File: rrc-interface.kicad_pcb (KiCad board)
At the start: 2 copper layers, 236.7 x 151.8 mm, 48 parts, among them J1 Mic Input, J10 Input Only Pins, J11 Input Only Pins, J12 Flash mode, J13 Switch Assembly, J2 8P8C_LED_Shielded, J3 6P6C RRC, J4 Audio Out, J5 Ptt, J6 TF Set, J7 UART2 Socket, J8 UART Socket, J9 SPI Breakout, U1 ESP32-DevKitC

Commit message: cont routing work
Changes:

* Added mounting holes
* Tried to trim down PCB size a litle more.
* Attempted to separate digital IO from analog.
* Added socket IC for RJ45 & 6P6C / RJ12 configurability.
* WIP: Add muxer for UART line switching.

Comment:

The muxer UART functionality isn't complete, the idea is to allow switching between using
the RJ45 RXD & TXD UART to the RJ12 / 6P6C UART lines.
Since the real rrc hardware supports this (depends on the radio configured) & maybe depending on socket strapping..
Need to add a jumper to enable switching between these, alternatively use a GPIO pin??
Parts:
- removed J7: UART2 Socket, Connector_Molex:Molex_KK-254_AE-6410-02A_1x02_P2.54mm_Vertical
- added C1: 0.1uF, Capacitor_SMD:C_0603_1608Metric, F.Cu at (61.8, 52.0)
- added C14: 0.1uF, Capacitor_SMD:C_0603_1608Metric, F.Cu at (101.0, 118.7)
- added C15: 0.1uF, Capacitor_SMD:C_0603_1608Metric, F.Cu at (41.2, 51.0)
- added C16: 0.1uF, Capacitor_SMD:C_0603_1608Metric, F.Cu at (50.2, 51.0)
- added C4: 0.1uF, Capacitor_SMD:C_0603_1608Metric, F.Cu at (131.2, 127.0)
- added J15: RRC Optional Config DIP Socket, Package_DIP:DIP-18_W7.62mm_Socket, F.Cu at (111.2, 106.0)
- added U2: ADP1108AN, Package_DIP:DIP-8_W7.62mm, F.Cu at (78.2, 145.9)
- added U3: ADG884xRM, Package_SO:MSOP-10_3x3mm_P0.5mm, F.Cu at (54.0, 115.8)
- J1: value Mic Input -> Mic Jack; footprint Connector_Audio:Jack_3.5mm_CUI_SJ1-3533NG_Horizontal -> Connector_Audio:Jack_3.5mm_CUI_SJ1-3523N_Horizontal
- J2: value 8P8C_LED_Shielded -> To RRC
- J5, J6: footprint Connector_Audio:Jack_3.5mm_CUI_SJ1-3533NG_Horizontal -> Connector_Audio:Jack_3.5mm_CUI_SJ1-3523N_Horizontal
- J9: footprint Connector_Molex:Molex_KK-254_AE-6410-06A_1x06_P2.54mm_Vertical -> Connector_PinSocket_2.54mm:PinSocket_1x06_P2.54mm_Vertical
- moved J12 198.9 mm to (30.5, 46.2), turned to -90 degrees
- moved C10 190.9 mm to (37.8, 31.5), turned to -90 degrees
- moved R12 178.4 mm to (40.3, 23.5), turned to 180 degrees
- moved C8 169.6 mm to (55.0, 30.2), turned to -90 degrees
- moved VFO1 167.5 mm to (28.7, 119.9), turned to -90 degrees
- moved C9 158.1 mm to (72.2, 30.3), turned to -90 degrees
- moved R10 154.0 mm to (57.6, 23.5), turned to 180 degrees
- moved C2 145.5 mm to (45.5, 141.2)
- moved R11 143.3 mm to (74.9, 23.5), turned to 180 degrees
- moved C1 137.6 mm to (130.2, 158.0), turned to 180 degrees
- moved J9 131.9 mm to (24.0, 76.0)
- moved J6 129.1 mm to (143.1, 153.2)
- moved J5 120.7 mm to (143.2, 121.8)
- moved C5 118.8 mm to (130.2, 154.2), turned to 180 degrees
- moved C6 117.5 mm to (106.8, 30.5), turned to -90 degrees
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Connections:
- C13 pad 1: +3V3 -> /GPIO 12
- C13 pad 2: GND -> Net-(U1-MTDI/GPIO12/ADC2_CH5)
- J10 pad 1: /GPIO 12 -> /GPIO 14
- J10 pad 2: /GPIO 14 -> /GPIO 12
- J11 pad 1: /GPIO 39 -> /GPIO 36
- J11 pad 2: /GPIO 36 -> /GPIO 39
- J13 pad 1: +3.3V -> +3V3
- J13 pad 3: Split -> Band
- J13 pad 4: Rit -> Mode
- J13 pad 5: Cycle mem -> Generic
- J13 pad 6: Mode -> Xit
- J13 pad 7: Band -> Cycle mem
- J13 pad 8: Generic -> Rit
- J13 pad 9: Xit -> Split
- J2 pad 1: unconnected-(J2-Pad1) -> PWR 8V
- J2 pad 2: unconnected-(J2-Pad2) -> TXD
- J2 pad 3: MIC -> SPK OUT
- J2 pad 4: MICE -> PTT
- J2 pad 5: PTT -> MICE
- J2 pad 6: GND -> Net-(C14-Pad1)
- J2 pad 7: /8V -> GND
- J2 pad 8: /UP -> RXD
- J3 pad 2: /8V -> PWR 8V
- J5 pad S: PTT -> Net-(C4-Pad1)
- J6 pad S: TF Set -> Net-(C5-Pad1)
- R14 pad 2: Xit -> Split
- R15 pad 2: Generic -> Rit
- R16 pad 2: Band -> Cycle mem
- R17 pad 2: Mode -> Xit
- R18 pad 2: Cycle mem -> Generic
- R19 pad 2: Rit -> Mode
- R20 pad 2: Split -> Band
- U1 pad 11: Split -> Cycle mem
- U1 pad 12: /GPIO 14 -> Net-(U1-MTMS/GPIO14/ADC2_CH6)
- U1 pad 13: /GPIO 12 -> Net-(U1-MTDI/GPIO12/ADC2_CH5)
- U1 pad 15: /Spare -> Net-(U1-MTCK/GPIO13/ADC2_CH4)
- U1 pad 27: /TDO -> /RDO
- U1 pad 28: /RDO -> /TDO
- U1 pad 30: /Encoder A -> /Encoder B
- U1 pad 31: /Encoder B -> /Encoder A
- U1 pad 34: /RX -> /TX
- U1 pad 35: /TX -> /RX
- U1 pad 36: Band -> Mode
- U1 pad 37: Mode -> Band
- U1 pad 7: /RF Gain -> Net-(U1-32K_XP/GPIO32/ADC1_CH4)
- U1 pad 9: Cycle mem -> Split
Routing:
- net GND: track 524.1 -> 22.1 mm, vias 10 -> 14
- net Generic: track 183.8 -> 51.1 mm, vias 2 -> 0
- net /TDO: track 188.4 -> 67.3 mm, vias 2 -> 0
- net /RF Gain: track 139.6 -> 33.3 mm
- net Band: track 141.7 -> 38.9 mm, vias 2 -> 0
- net RXD: track 0.00 -> 99.3 mm, vias 0 -> 3
- net /RDO: track 171.3 -> 78.9 mm
- net TXD: track 0.00 -> 92.4 mm, vias 0 -> 2
- net /AF Gain: track 125.6 -> 33.4 mm
- net MICE: track 23.3 -> 99.9 mm
- net Xit: track 140.9 -> 70.1 mm, vias 2 -> 0
- net Split: track 116.0 -> 55.4 mm, vias 1 -> 0
- net Rit: track 120.4 -> 60.0 mm
- net Cycle mem: track 120.4 -> 67.1 mm, vias 2 -> 0
- net SPK OUT: track 0.00 -> 41.0 mm
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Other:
- board size 236.7 x 151.8 mm -> 147.5 x 152.2 mm
- board text added: "Step up converter"
- board text added: "UART selector"
- board text added: "locked"

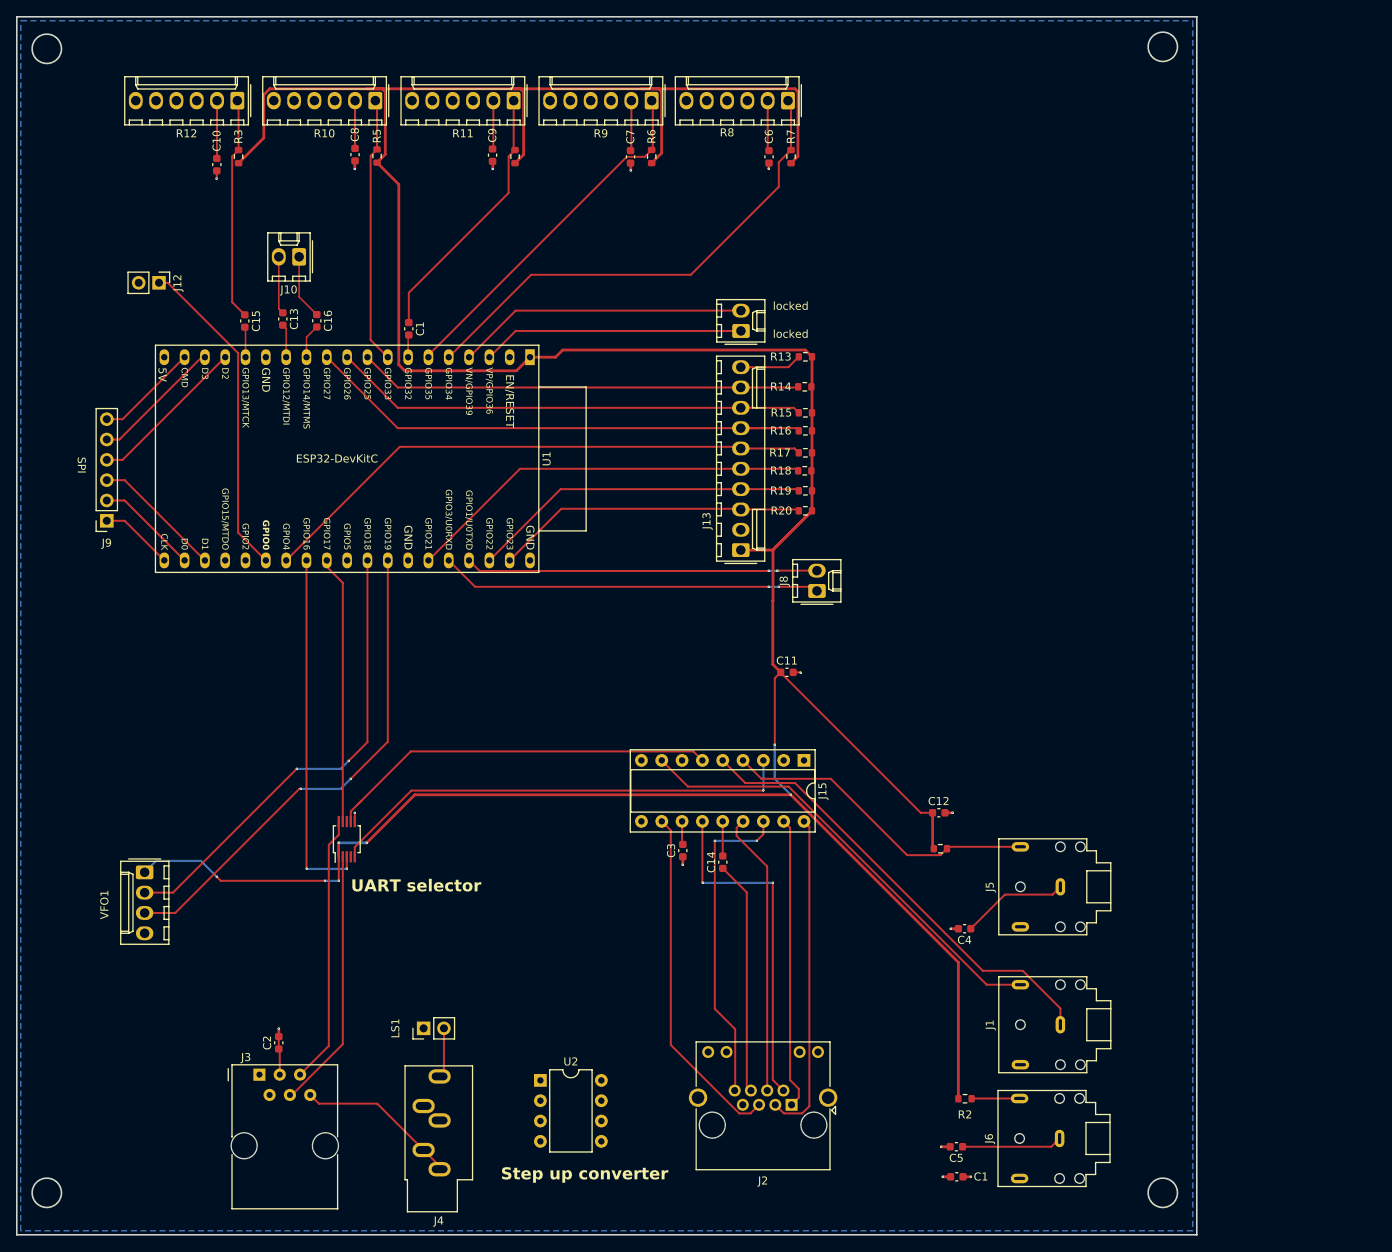
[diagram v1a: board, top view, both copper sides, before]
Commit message: add gnd pour to top layer, try to optimize routing
Changes:

* Opt to use normal via's instead of micro via's to reduce cost / production time.
* Add ground pour / plane to top layer.
* Reorganize component layout a bit to try to optimize paths.
* Change connector types to JST (will soon have a crimp kit for these connectors).
* Try to split the PCB into analog and digital sections.
* Add mounting holes.
* Increase track size for power traces.

TODO:

* Via stitching to make sure the resistance between planes is as low as possible?
* Configure board size.
* Finish variable resistor PCB's & add connectors to the PCB's for interconnect.
* Remove 3.5mm jacks from layout, need separate PCB's for these. Need to be able to mount the jack's on a panel, need flexibility.
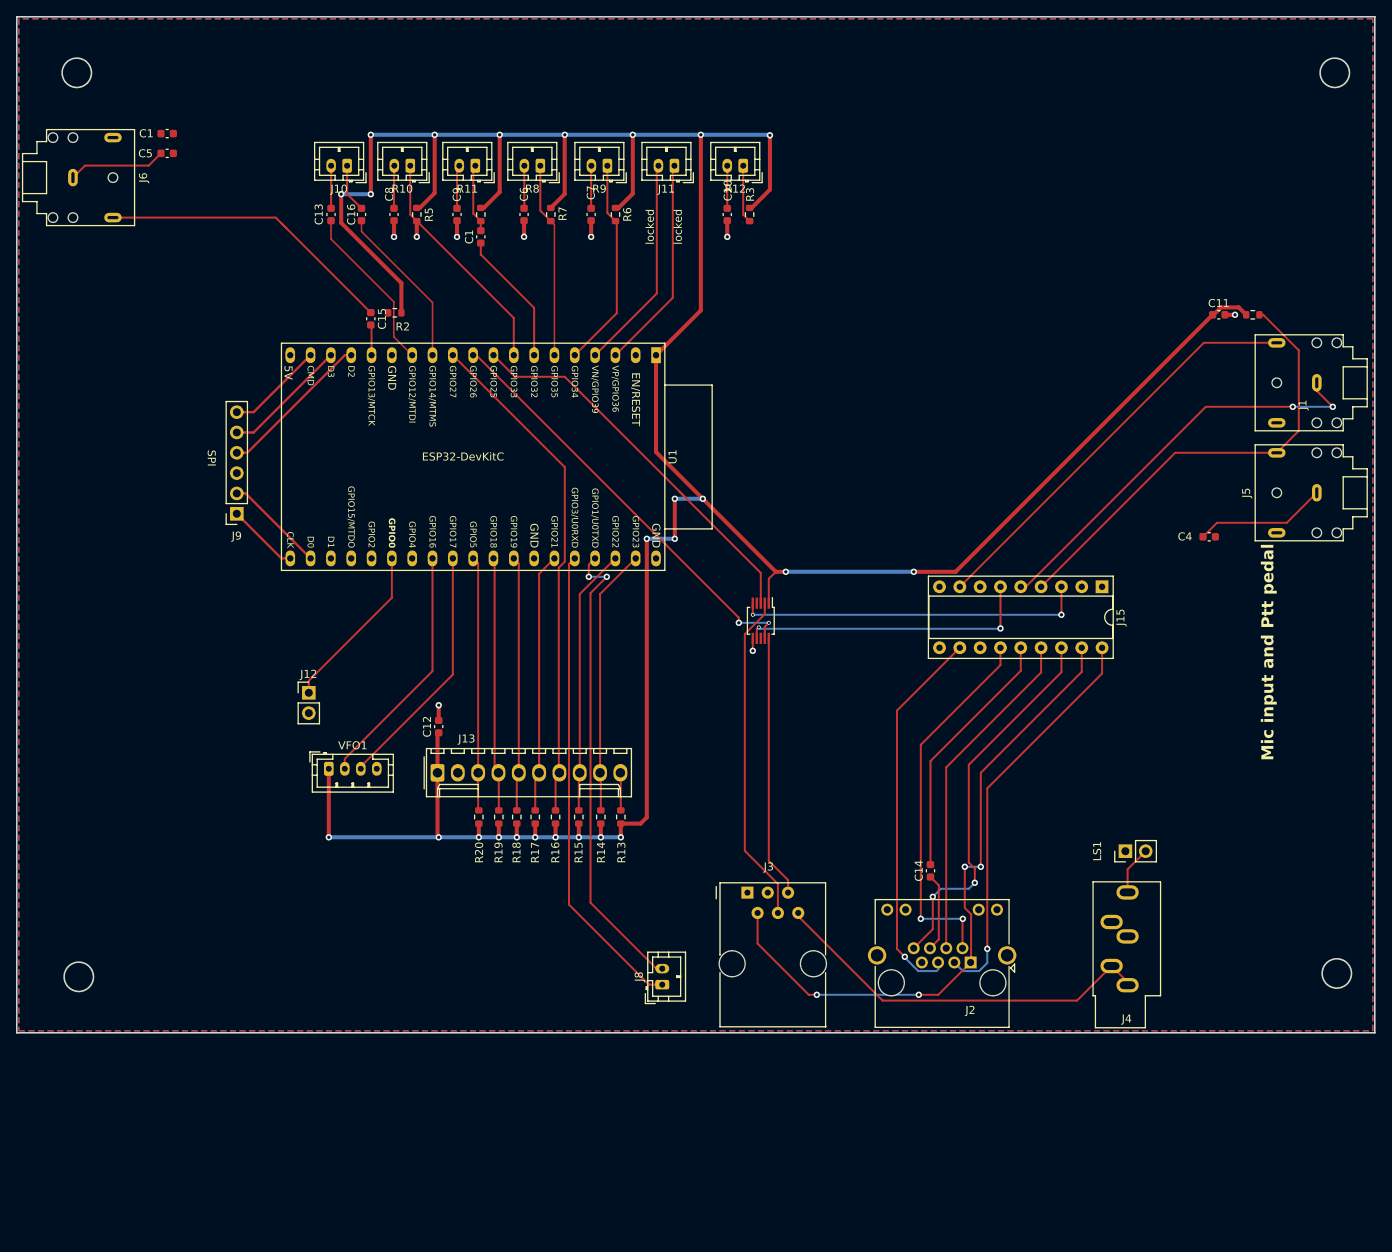
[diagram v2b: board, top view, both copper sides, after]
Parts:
- removed C2, C3: 0.1uF, Capacitor_SMD:C_0603_1608Metric
- removed U2: ADP1108AN, Package_DIP:DIP-8_W7.62mm
- J10, J11, J8: footprint Connector_Molex:Molex_KK-254_AE-6410-02A_1x02_P2.54mm_Vertical -> Connector_JST:JST_PH_B2B-PH-K_1x02_P2.00mm_Vertical
- R10, R11, R12, R8, R9: footprint Connector_Molex:Molex_KK-254_AE-6410-06A_1x06_P2.54mm_Vertical -> Connector_JST:JST_PH_B2B-PH-K_1x02_P2.00mm_Vertical
- VFO1: footprint Connector_Molex:Molex_KK-254_AE-6410-04A_1x04_P2.54mm_Vertical -> Connector_JST:JST_PH_B4B-PH-K_1x04_P2.00mm_Vertical
- moved J6 172.2 mm to (19.8, 33.1), turned to -90 degrees
- moved C1 163.5 mm to (31.5, 27.6), turned to 0 degrees
- moved C5 158.6 mm to (31.5, 30.1), turned to 0 degrees
- moved R2 121.4 mm to (60.0, 50.0), turned to 0 degrees
- moved LS1 90.5 mm to (151.3, 117.3)
- moved J4 89.0 mm to (151.6, 134.1)
- moved J1 86.4 mm to (175.2, 58.8)
- moved R1 77.3 mm to (167.2, 50.2)
- moved C11 70.1 mm to (163.0, 50.2)
- moved J3 65.1 mm to (104.1, 122.5)
- moved R3 64.3 mm to (104.4, 37.7), turned to -90 degrees
- moved C10 64.1 mm to (101.6, 37.7)
- moved R12 63.8 mm to (103.6, 31.6)
- moved C12 63.4 mm to (65.5, 101.7), turned to 90 degrees
- moved R13 62.0 mm to (88.2, 113.0), turned to 90 degrees
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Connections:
- C1 pad 1: /RF Gain -> Net-(U1-32K_XP/GPIO32/ADC1_CH4)
- C1 pad 2: Net-(U1-32K_XP/GPIO32/ADC1_CH4) -> /RF Gain
- C15 pad 1: /Spare -> TF Set
- J13 pad 3: Band -> Generic
- J13 pad 4: Mode -> Split
- J13 pad 5: Generic -> Mode
- J13 pad 9: Split -> Band
- R14 pad 2: Split -> Band
- R18 pad 2: Generic -> Mode
- R19 pad 2: Mode -> Split
- R20 pad 2: Band -> Generic
- U1 pad 10: Rit -> /TDO
- U1 pad 26: Xit -> unconnected-(U1-ADC2_CH0/GPIO4-Pad26)
- U1 pad 27: /RDO -> /Encoder B
- U1 pad 28: /TDO -> /Encoder A
- U1 pad 29: unconnected-(U1-GPIO5-Pad29) -> Generic
- U1 pad 30: /Encoder B -> Split
- U1 pad 31: /Encoder A -> Mode
- U1 pad 33: Generic -> Xit
- U1 pad 36: Mode -> Rit
- U1 pad 5: /Rit/Xit Value -> /IF Shift
- U1 pad 6: /IF Shift -> /Rit/Xit Value
- U1 pad 9: Split -> /RDO
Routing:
- net +3V3: track 439.0 -> 393.7 mm, vias 7 -> 25
- net PWR 8V: track 37.4 -> 81.7 mm, vias 0 -> 4
- net Xit: track 70.1 -> 32.5 mm
- net /Rit/Xit Value: track 61.6 -> 24.4 mm
- net /Encoder A: track 62.8 -> 31.1 mm, vias 2 -> 0
- net TF Set: track 6.01 -> 37.6 mm
- net AF: track 19.8 -> 49.0 mm
- net /Encoder B: track 58.4 -> 30.8 mm, vias 2 -> 0
- net Rit: track 60.0 -> 33.4 mm
- net /RF Gain: track 33.3 -> 8.37 mm
- net PTT: track 75.6 -> 99.9 mm
- net Split: track 55.4 -> 31.8 mm
- net MIC: track 61.4 -> 83.9 mm, vias 0 -> 2
- net /Spare: track 27.8 -> 7.25 mm
- net /Boot / Flash: track 40.9 -> 21.1 mm
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- added copper zone on F.Cu, net GND
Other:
- board size 147.5 x 152.2 mm -> 169.8 x 127 mm
- board text added: "Mic input and Ptt pedal"
- board text removed: "Step up converter"
- board text removed: "UART selector"
